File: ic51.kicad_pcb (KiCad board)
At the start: 2 copper layers, 5 parts, among them J1 Conn_02x18_Odd_Even, J2 Conn_02x18_Odd_Even, J3 Conn_02x18_Odd_Even, J4 Conn_02x18_Odd_Even, U1 ic51-1444-schem

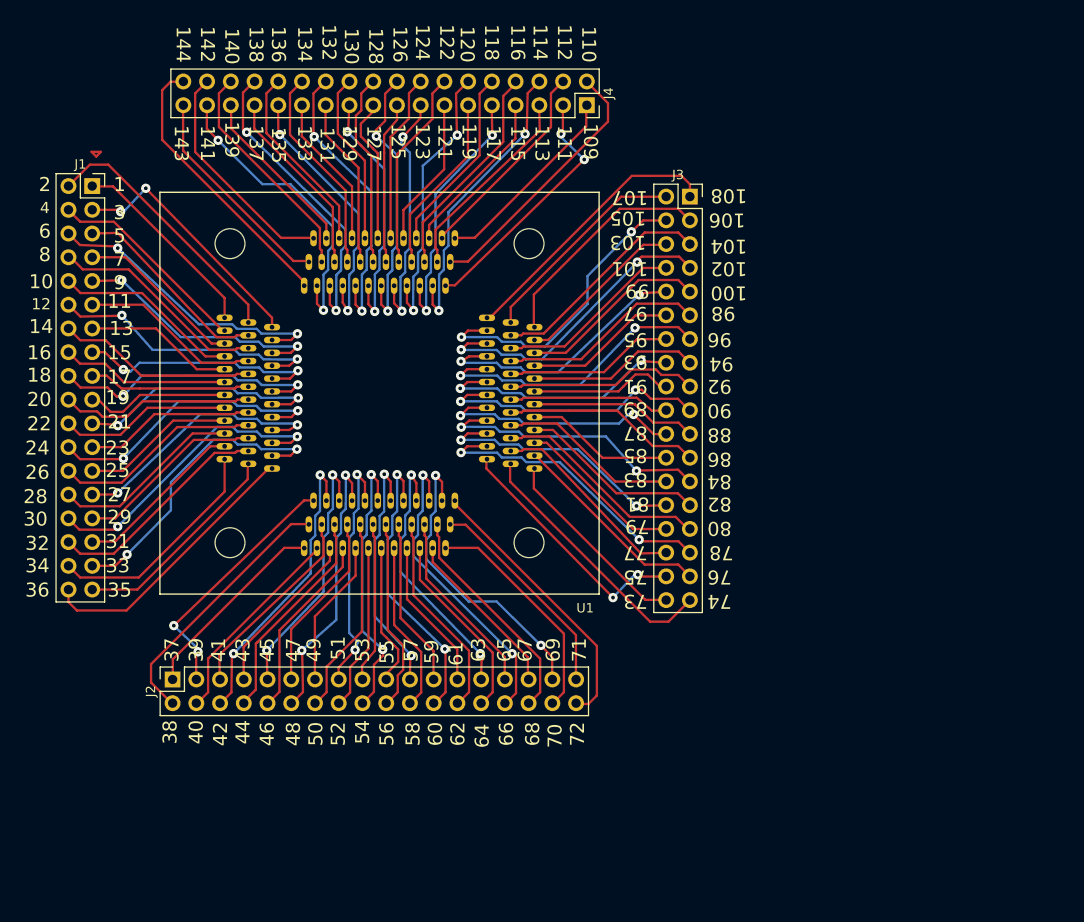
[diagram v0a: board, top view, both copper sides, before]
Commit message: swap F and B copper layer, increase trace width around vias to 1.2mm
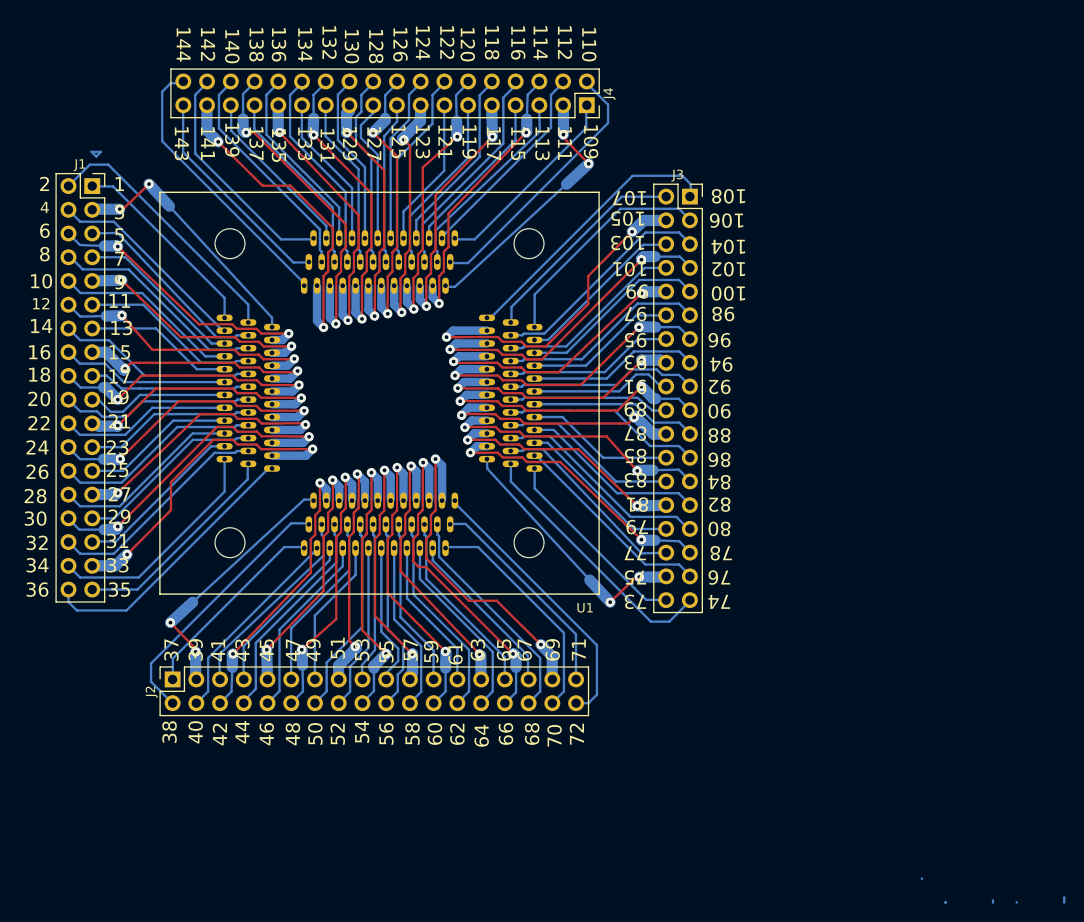
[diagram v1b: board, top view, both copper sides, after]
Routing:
- net /138: track 33.1 -> 36.6 mm
- net /69: track 32.6 -> 36.0 mm
- net /33: track 32.6 -> 36.0 mm
- net /105: track 32.6 -> 36.0 mm
- net /141: track 32.6 -> 36.0 mm
- net /66: track 33.1 -> 36.5 mm
- net /30: track 33.1 -> 36.0 mm
- net /102: track 33.1 -> 36.0 mm
- net /99: track 28.7 -> 30.6 mm
- net /27: track 28.7 -> 30.6 mm
- net /135: track 28.8 -> 30.6 mm
- net /63: track 28.9 -> 30.6 mm
- net /78: track 31.9 -> 30.3 mm
- net /114: track 31.9 -> 30.3 mm
- net /42: track 31.8 -> 30.3 mm
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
